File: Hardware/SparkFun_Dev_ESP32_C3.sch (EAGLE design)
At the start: 47 parts, among them J1 USB Female Type C Connector, J4 QWIIC_RIGHT_ANGLE, Q1 20V/4.2A/52mΩ/1.4W, U1 ESP32-C3, U2 RT9080-33GJ5

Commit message: Shrinks design
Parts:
- removed D3: 1A/23V/620mV, SparkFun-DiscreteSemi:DIODE-SCHOTTKY-BAT20J
- removed H3, H4: STAND-OFF, SparkFun-Hardware:STAND-OFF
- removed LOGO2: OSHW-LOGOS, SparkFun-Aesthetics:OSHW-LOGOS
- removed Q1: 20V/4.2A/52mΩ/1.4W, SparkFun-DiscreteSemi:MOSFET_PCH-DMG2305UX-7
- removed R13, R14, R7: 100k, SparkFun-Resistors:100KOHM-0402T-1/16W-1%
- BOOT, RESET: value MOMENTARY-SWITCH-SPST-SMD-4.6X2.8MM -> MOMENTARY-SWITCH-SPST-SMD-6.0X3.5MM; device SparkFun-Switches:MOMENTARY-SWITCH-SPST-SMD-4.6X2.8MM -> SparkFun-Switches:MOMENTARY-SWITCH-SPST-SMD-6.0X3.5MM
- J2, J3: device SparkFun-Connectors:CONN_06NO_SILK_NO_POP -> SparkFun-Connectors:CONN_041X04_NO_SILK_NO_POP
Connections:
- removed net IO1/V_BATT_2: R13.1, R14.2
- removed net IO18: J3.5
- removed net IO19: J3.6
- removed net IO2: J2.3
- removed net IO3: J2.4
- removed net IO4: J2.5
- removed net IO5: J2.6
- removed net N$9: C1.1, D3.C, Q1.S, R8.1, U2.IN
- removed net V_BATT: J3.1, Q1.D, R13.2
- net 3.3V: no longer J2.2
- net GND: no longer J2.1, R14.1, R7.1
- net IO20/TX: no longer J3.3
- net IO21/RX: no longer J3.4
- net V_USB: now also C1.1, R8.1, U2.IN; no longer D3.A, J3.2, Q1.G, R7.2
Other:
- note removed: "Battery Voltage"
- moved on the sheet: C1, C2, D1, D2, PWR, R1, R2, R8, U2

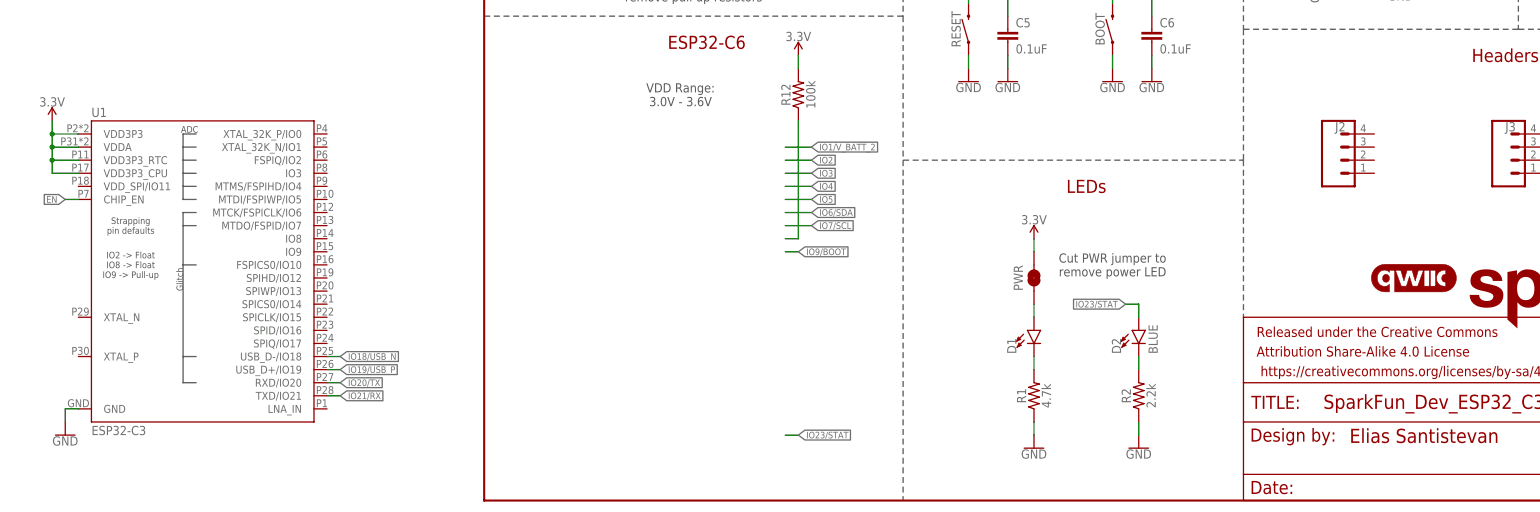
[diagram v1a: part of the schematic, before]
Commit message: Adds crystal
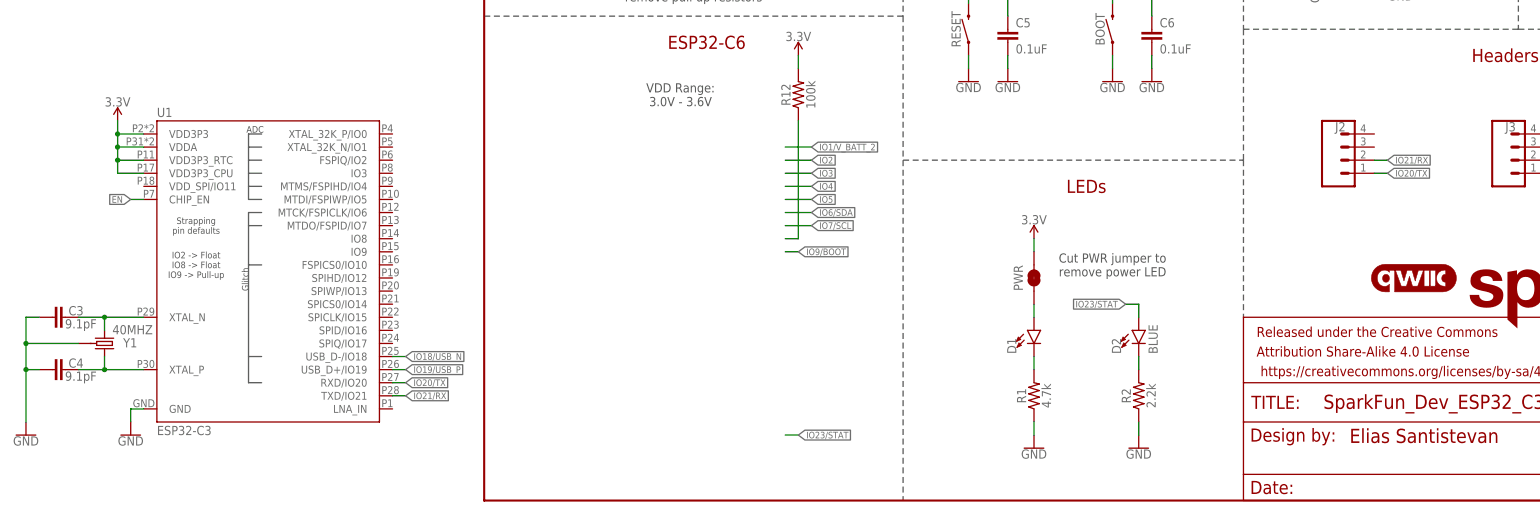
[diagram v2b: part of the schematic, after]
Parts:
- added C3, C4: 9.1pF, SparkFun-Capacitors:9.1PF-0402-TIGHT
- added Y1: 40MHZ, SparkFun-Clocks:CRYSTAL-40MHZ-SMD-2X2.5MM
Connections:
- new net N$10: C4.2, U1.XTAL_P, Y1.2
- new net N$9: C3.2, U1.XTAL_N, Y1.1
- net GND: now also C3.1, C4.1, Y1.GND
- net IO20/TX: now also J2.1
- net IO21/RX: now also J2.2
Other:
- moved on the sheet: U1

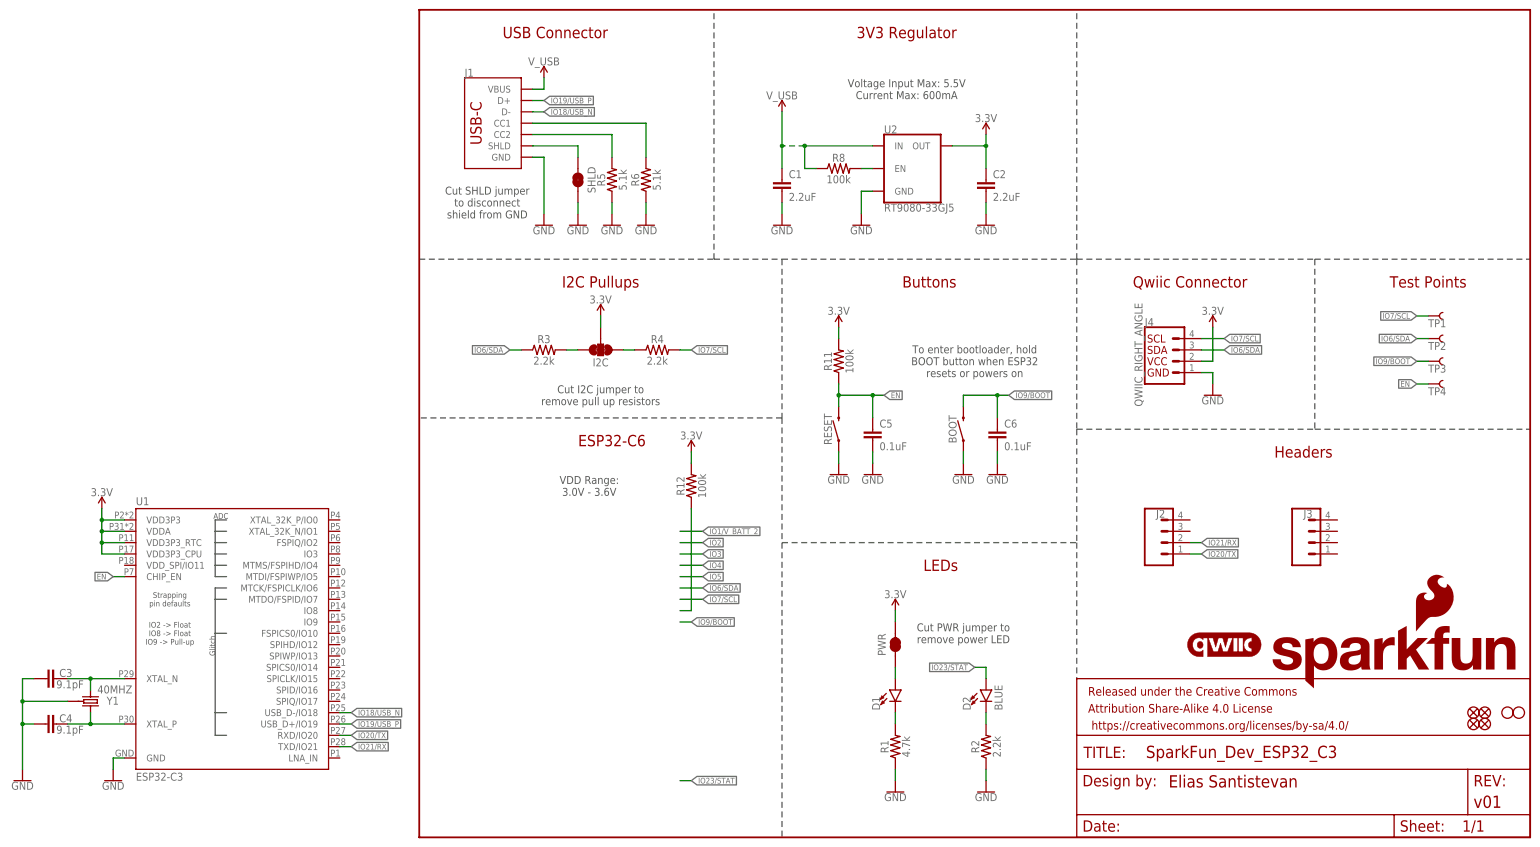
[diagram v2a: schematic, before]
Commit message: Adds more documentation, decoupling caps, antennas, rearranges schematic
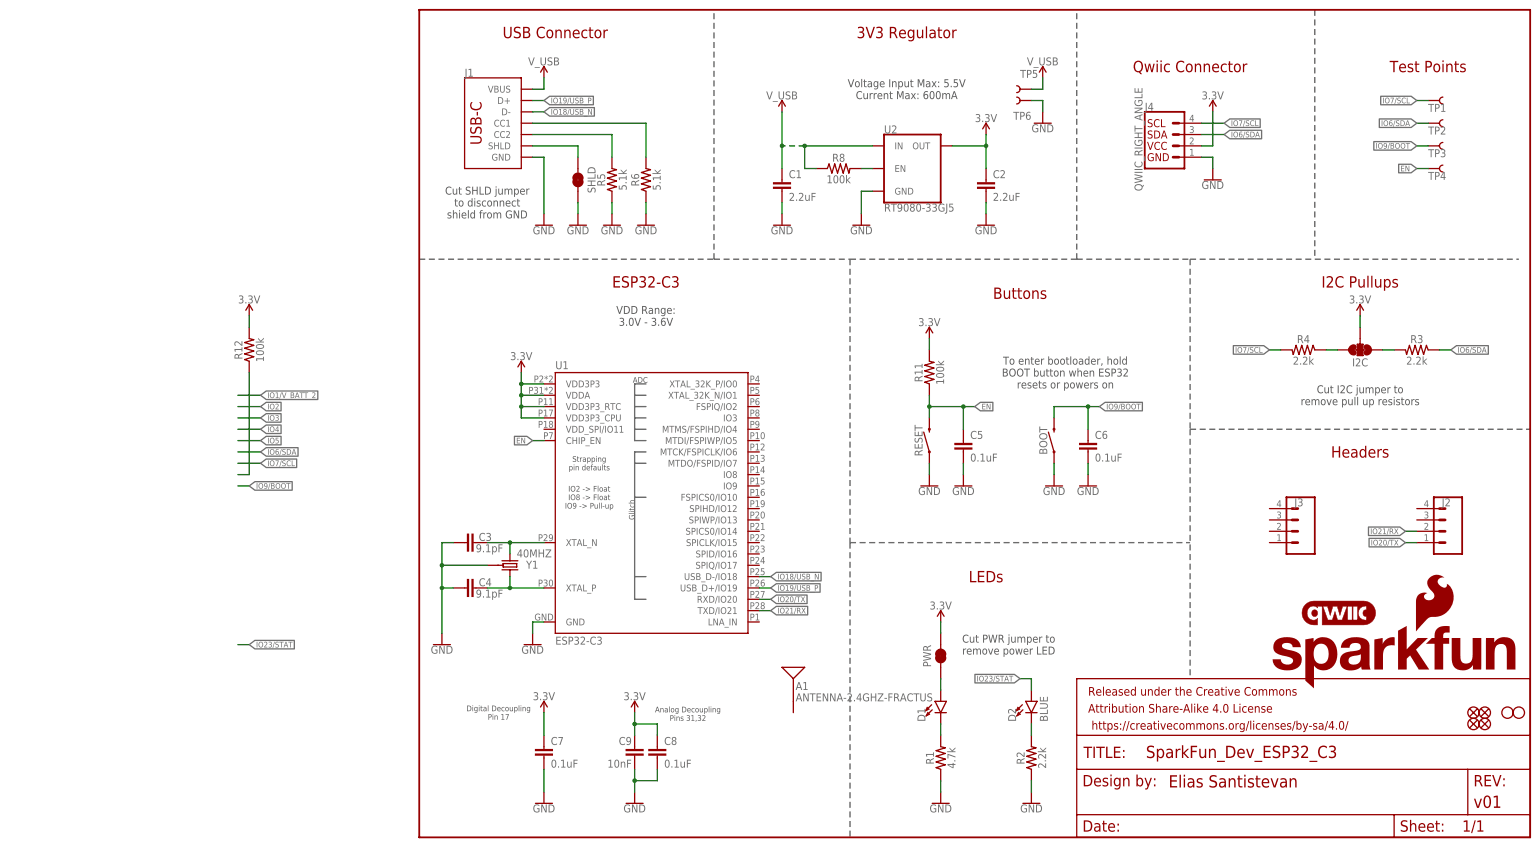
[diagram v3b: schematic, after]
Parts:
- added A1: ANTENNA-2.4GHZ-FRACTUS, SparkFun-RF:ANTENNA-2.4GHZ-FRACTUS
- added C7, C8: 0.1uF, SparkFun-Capacitors:0.1UF-0402T-16V-10%
- added C9: 10nF, SparkFun-Capacitors:10NF-0402T-25V-10%
- added TP5, TP6: TEST-POINT3X5, SparkFun-Connectors:TEST-POINT3X5
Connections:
- net 3.3V: now also C7.1, C8.1, C9.1
- net GND: now also C7.2, C8.2, C9.2, TP6.1
- net V_USB: now also TP5.1
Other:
- note added: "Analog Decoupling Pins 31,32"
- note added: "Digital Decoupling Pin 17"
- note added: "ESP32-C3"
- note removed: "ESP32-C6"
- moved on the sheet: BOOT, C3, C4, C5, C6, D1, D2, I2C, J2, J3, J4, PWR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

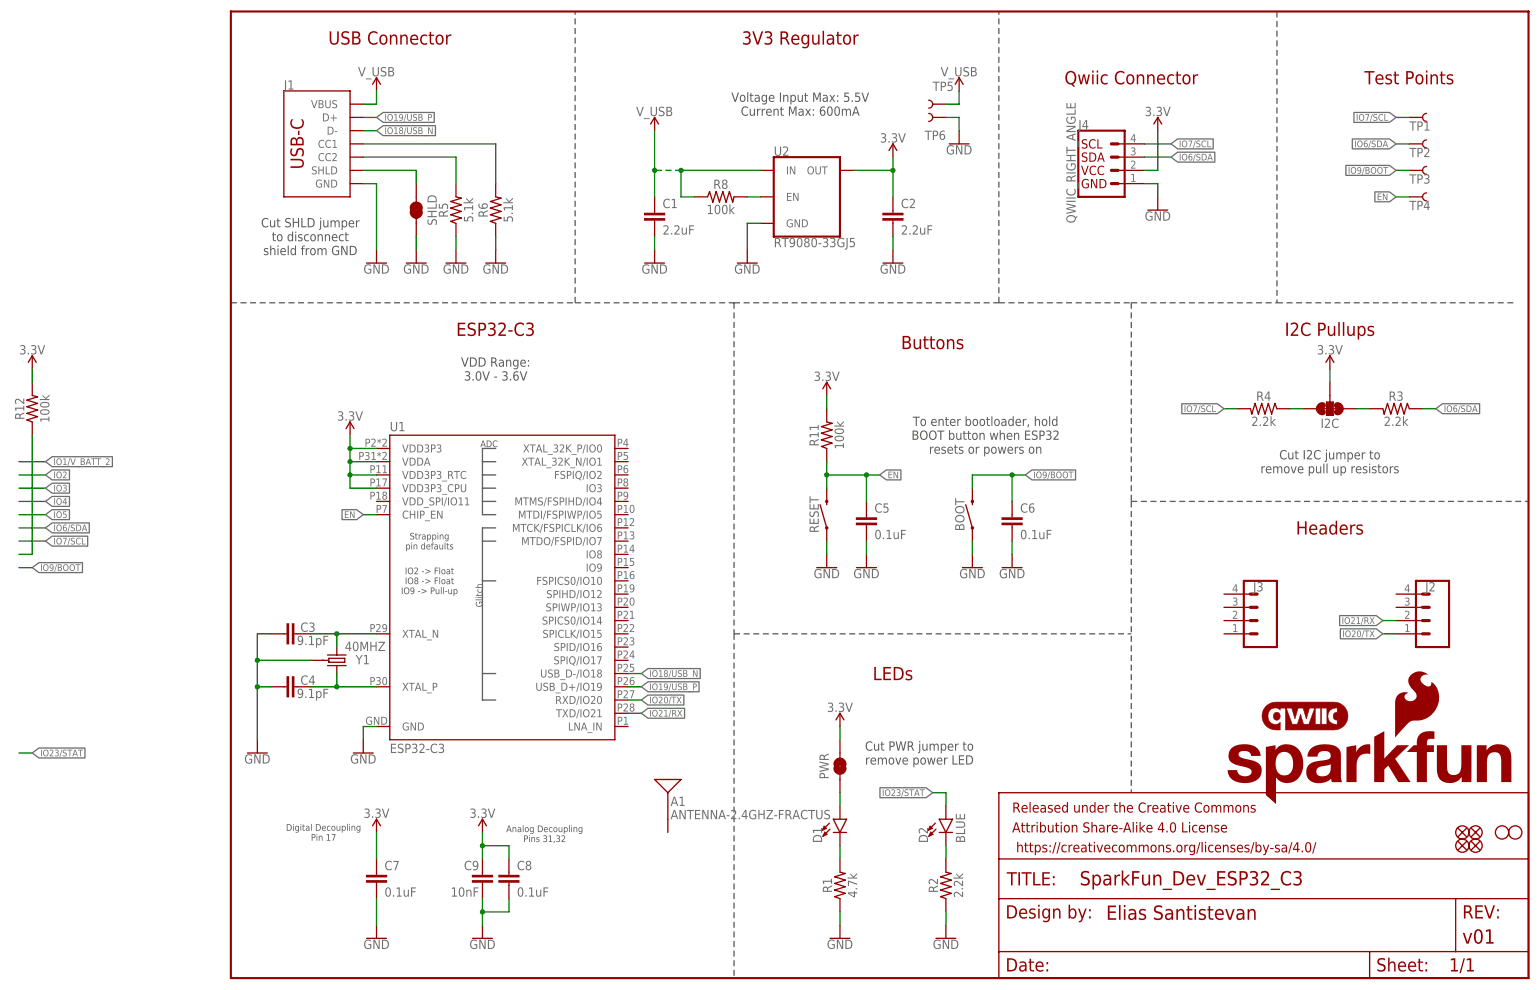
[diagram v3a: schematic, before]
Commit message: Adds new antenna, nets IO, removes STAT LED
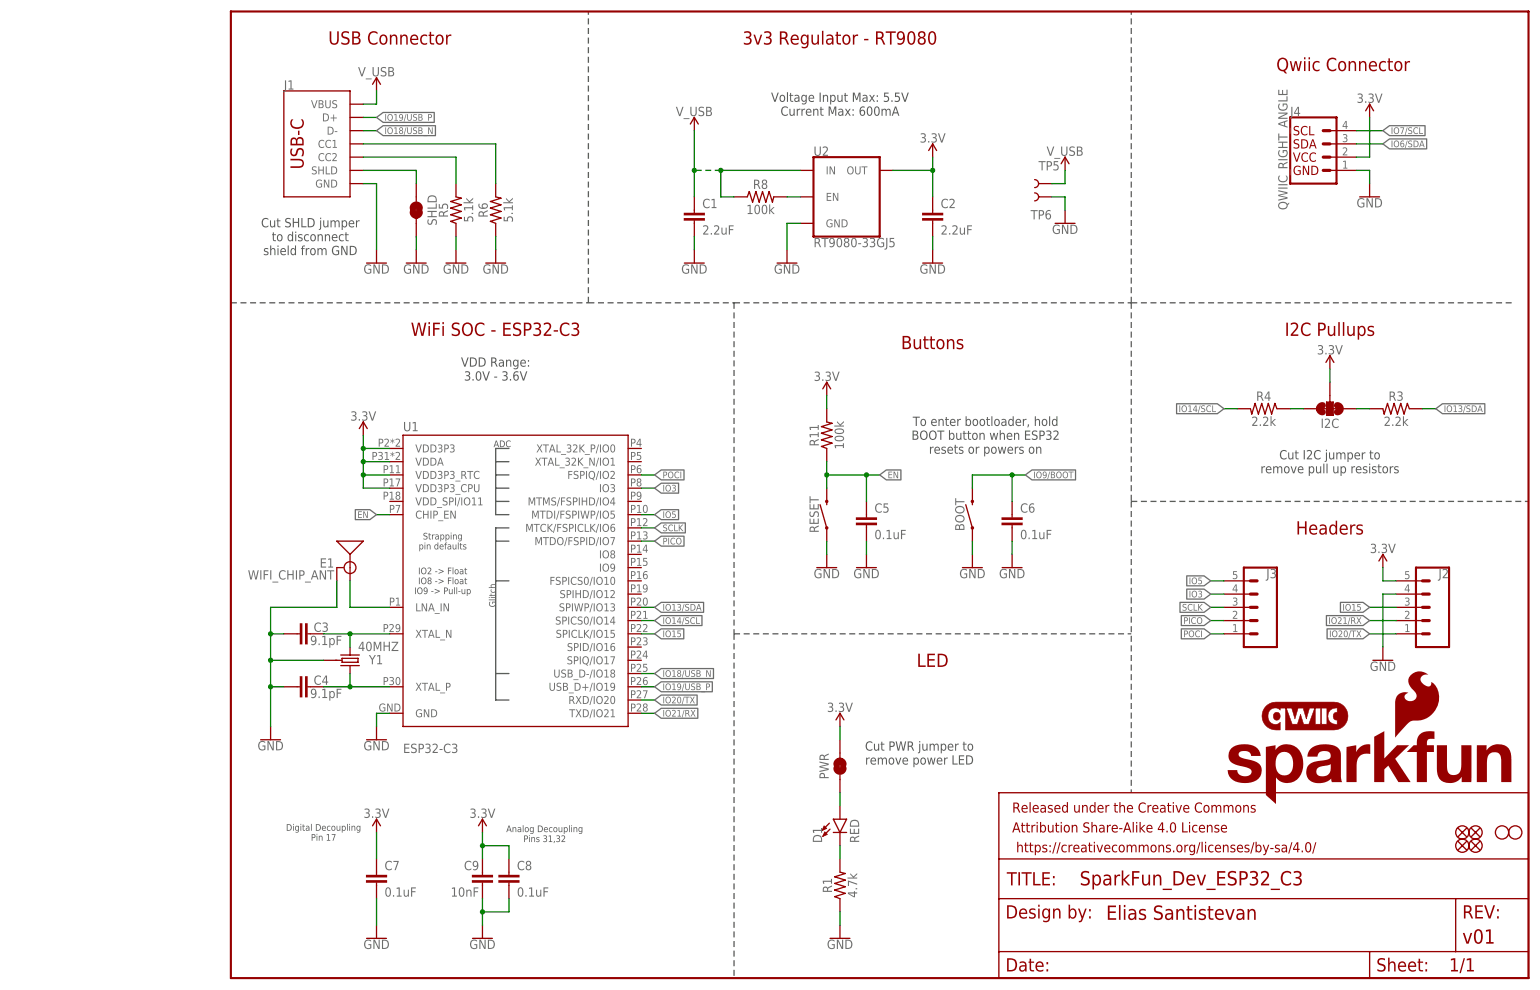
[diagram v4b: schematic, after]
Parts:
- removed A1: ANTENNA-2.4GHZ-FRACTUS, SparkFun-RF:ANTENNA-2.4GHZ-FRACTUS
- removed D2: BLUE, SparkFun-LED:LED-BLUE0603
- removed R12: 100k, SparkFun-Resistors:100KOHM-0402T-1/16W-1%
- removed R2: 2.2k, SparkFun-Resistors:2.2KOHM-0402T-1/16W-1%
- removed TP1, TP2, TP3, TP4: TEST-POINT3, SparkFun-Connectors:TEST-POINT3
- added E1: WIFI_CHIP_ANT, ESP32-C3-MINI-1:WIFI_CHIP_ANT
- BOOT, RESET: value MOMENTARY-SWITCH-SPST-SMD-6.0X3.5MM -> MOMENTARY-SWITCH-SPST-SMD-4.6X2.8MM; device SparkFun-Switches:MOMENTARY-SWITCH-SPST-SMD-6.0X3.5MM -> SparkFun-Switches:MOMENTARY-SWITCH-SPST-SMD-4.6X2.8MM
- D1: value (none) -> RED; device SparkFun-LED:LED-RED_0603-KB -> SparkFun-LED:LED-RED_0402
- J2, J3: device SparkFun-Connectors:CONN_041X04_NO_SILK_NO_POP -> SparkFun-Connectors:CONN_05NO_SILK
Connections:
- removed net IO23/STAT: D2.A
- removed net N$14: R12.1
- removed net N$3: D2.C, R2.2
- new net IO13/SDA: R3.1, U1.SPIWP/IO13
- new net IO14/SCL: R4.2, U1.SPICS0/IO14
- new net IO15: J2.3, U1.SPICLK/IO15
- new net IO3: J3.4, U1.IO3
- new net IO5: J3.5, U1.MTDI/FSPIWP/IO5
- new net N$11: E1.SIGNAL, U1.LNA_IN
- new net PICO: J3.2, U1.MTDO/FSPID/IO7
- new net POCI: J3.1, U1.FSPIQ/IO2
- new net SCLK: J3.3, U1.MTCK/FSPICLK/IO6
- net 3.3V: now also J2.5; no longer R12.2
- net EN: no longer TP4.1
- net GND: now also E1.GND, J2.4; no longer R2.1
- net IO6/SDA: no longer R3.1, TP2.1
- net IO7/SCL: no longer R4.2, TP1.1
- net IO9/BOOT: no longer TP3.1
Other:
- note added: "3v3 Regulator - RT9080"
- note added: "LED"
- note added: "WiFi SOC - ESP32-C3"
- note removed: "3V3 Regulator"
- note removed: "ESP32-C3"
- note removed: "LEDs"
- note removed: "Test Points"
- moved on the sheet: C1, C2, C3, C4, J4, R8, TP5, TP6, U1, U2, Y1

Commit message: Moves towards Pro Micro form factor
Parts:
- removed FD1, FD2, FD3, FD4: FIDUCIALUFIDUCIAL, SparkFun-Aesthetics:FIDUCIALUFIDUCIAL
- removed FRAME1: FRAME-LETTER, SparkFun-Aesthetics:FRAME-LETTER
- removed H1, H2: STAND-OFF, SparkFun-Hardware:STAND-OFF
- removed J2, J3: (no value), SparkFun-Connectors:CONN_05NO_SILK
- removed LOGO3: QWIIC_LOGO_3MM, SparkFun-Aesthetics:QWIIC_LOGO_3MM
- removed TP5, TP6: TEST-POINT3X5, SparkFun-Connectors:TEST-POINT3X5
- added FRAME2: FRAME-LEDGER, SparkFun-Aesthetics:FRAME-LEDGER
- added J5, J6: (no value), Castellated:CONN_12CASTLE
- added JP14: USB_SOLDER_PADS, SparkFun-Connectors:USB_SOLDER_PADS
- added TP3: TEST-POINT3X5, SparkFun-Connectors:TEST-POINT3X5
- added U3: WS2812-2020, SparkFun-LED:WS2812-2020
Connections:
- new net !RESET!: J6.3
- new net 0/TX0: J5.12
- new net 1/RX0: J5.11
- new net 2: J5.8
- new net 20/SPI_CIPO: J6.10
- new net 21/SPI_!CS!: J6.12
- new net 22/SPI_SCK: J6.9
- new net 23/SPI_COPI: J6.11
- new net 25/WS2812-DI: U3.DI
- new net 3: J5.7
- new net 4: J5.6
- new net 5: J5.5
- new net 6: J5.4
- new net 7: J5.3
- new net 8/TX1: J5.2
- new net 9/RX1: J5.1
- new net A0: J6.8
- new net A1: J6.7
- new net A2: J6.6
- new net A3: J6.5
- new net GND1: JP14.4
- new net N$3: TP3.1, U3.DO
- new net RAW: J6.1, U3.VDD
- new net RP_D+: JP14.3
- new net RP_D-: JP14.2
- net 3.3V: now also J6.4; no longer J2.5
- net GND: now also J5.10, J5.9, J6.2, U3.VSS; no longer J2.4, TP6.1
- net IO15: no longer J2.3
- net IO20/TX: no longer J2.1
- net IO21/RX: no longer J2.2
- net IO3: no longer J3.4
- net IO5: no longer J3.5
- net PICO: no longer J3.2
- net POCI: no longer J3.1
- net SCLK: no longer J3.3
- net V_USB: now also JP14.1; no longer TP5.1
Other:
- moved on the sheet: BOOT, C1, C2, C3, C4, C5, C6, C7, C8, C9, D1, E1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
